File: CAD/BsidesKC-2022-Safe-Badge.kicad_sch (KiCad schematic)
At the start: 48 parts, among them J1 JTAG, J2 Conn_01x02_Female, J3 Conn_01x02_Female, J4 USB_B_Mini, J5 Conn_01x02_Female, SW1 SW_SPDT, SW2 SW_SPST, SW3 RotaryEncoder_Switch, U1 LTC4054, U2 ESP32-S2-WROVER, U3 CH330N, U4 TLV1117-33, X1 Badgelife_sao_connector_v169b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

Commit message: fixing footprint and fill
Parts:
- removed D21, D22: LED, BadgePiratesCommon:LED_Osram_Lx_P47F_D2mm_ReverseMount_Proper_Mask Only, symbol Device:LED
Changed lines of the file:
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@@
     (comment 3 "USB to Serial Connector")
-  )
-  (junction (at 55.88 158.75) (diameter 0) (color 0 0 0 0)
-  )
-  (junction (at 54.61 198.12) (diameter 0) (color 0 0 0 0)
   )
   (junction (at 36.83 198.12) (diameter 0) (color 0 0 0 0)
@@
     (stroke (width 0) (type default) (color 0 0 0 0))
   )
-  (wire (pts (xy 54.61 198.12) (xy 72.39 198.12))
-    (stroke (width 0) (type default) (color 0 0 0 0))
-  )
   (wire (pts (xy 25.4 96.52) (xy 44.45 96.52))
     (stroke (width 0) (type default) (color 0 0 0 0))
@@
     (stroke (width 0) (type default) (color 0 0 0 0))
   )
-  (wire (pts (xy 72.39 198.12) (xy 72.39 189.23))
-    (stroke (width 0) (type default) (color 0 0 0 0))
-  )
   (wire (pts (xy -30.48 173.99) (xy -12.7 173.99))
     (stroke (width 0) (type default) (color 0 0 0 0))
@@
     (stroke (width 0) (type default) (color 0 0 0 0))
   )
-  (wire (pts (xy 73.66 158.75) (xy 73.66 149.86))
-    (stroke (width 0) (type default) (color 0 0 0 0))
-  )
   (wire (pts (xy 72.39 179.07) (xy 72.39 170.18))
     (stroke (width 0) (type default) (color 0 0 0 0))
@@
   )
   (wire (pts (xy -48.26 173.99) (xy -38.1 173.99))
-    (stroke (width 0) (type default) (color 0 0 0 0))
-  )
-  (wire (pts (xy 55.88 158.75) (xy 73.66 158.75))
     (stroke (width 0) (type default) (color 0 0 0 0))
   )
@@
     )
   )
-  (global_label "IO13" (shape input) (at 81.28 149.86 0) (fields_autoplaced)
-    (effects (font (size 1.27 1.27)) (justify left))
-    (property "Intersheet References" "${INTERSHEET_REFS}" (id 0) (at 0 0 0)
-      (effects (font (size 1.27 1.27)) hide)
-    )
-  )
   (global_label "Boot" (shape input) (at 85.09 33.02 180) (fields_autoplaced)
     (effects (font (size 1.27 1.27)) (justify right))
@@
     (property "Intersheet References" "${INTERSHEET_REFS}" (id 0) (at 0 0 0)
       (effects (font (size 1.27 1.27)) hide)
-    )
-  )
-  (global_label "IO38" (shape input) (at 80.01 189.23 0) (fields_autoplaced)
-    (effects (font (size 1.27 1.27)) (justify left))
-    (property "Intersheet References" "${INTERSHEET_REFS}" (id 0) (at 86.6885 189.1506 0)
-      (effects (font (size 1.27 1.27)) (justify left) hide)
     )
   )
@@
     (pin "2")
   )
-  (symbol (lib_id "Device:LED") (at 77.47 149.86 0) (unit 1)
-    (in_bom yes) (on_board yes)
-    (property "Reference" "D22" (id 0) (at 77.2922 144.3482 0))
-    (property "Value" "LED" (id 1) (at 77.2922 146.6596 0))
-    (property "Footprint" "BadgePiratesCommon:LED_Osram_Lx_P47F_D2mm_ReverseMount_Proper_Mask Only" (id 2) (at 77.47 149.86 0)
-      (effects (font (size 1.27 1.27)) hide)
-    )
-    (property "Datasheet" "~" (id 3) (at 77.47 149.86 0)
-      (effects (font (size 1.27 1.27)) hide)
-    )
-    (pin "1")
-    (pin "2")
-  )
   (symbol (lib_id "power:GND") (at 152.4 101.6 0) (unit 1)
     (in_bom yes) (on_board yes)
@@
     (pin "2")
   )
-  (symbol (lib_id "Device:LED") (at 76.2 189.23 0) (unit 1)
-    (in_bom yes) (on_board yes)
-    (property "Reference" "D21" (id 0) (at 76.0222 183.7182 0))
-    (property "Value" "LED" (id 1) (at 76.0222 186.0296 0))
-    (property "Footprint" "BadgePiratesCommon:LED_Osram_Lx_P47F_D2mm_ReverseMount_Proper_Mask Only" (id 2) (at 76.2 189.23 0)
-      (effects (font (size 1.27 1.27)) hide)
-    )
-    (property "Datasheet" "~" (id 3) (at 76.2 189.23 0)
-      (effects (font (size 1.27 1.27)) hide)
-    )
-    (pin "1")
-    (pin "2")
-  )
   (symbol (lib_id "BadgePirates:Badgelife_sao_connector_v169bis") (at 217.17 139.7 0) (unit 1)
     (in_bom yes) (on_board yes) (fields_autoplaced)
@@
       (reference "D20") (unit 1) (value "LED") (footprint "BadgePiratesCommon:LED_Osram_Lx_P47F_D2mm_ReverseMount_Proper_Mask Only")
     )
-    (path "/9071e38a-572a-4eb6-923e-9269f884d02e"
-      (reference "D21") (unit 1) (value "LED") (footprint "BadgePiratesCommon:LED_Osram_Lx_P47F_D2mm_ReverseMount_Proper_Mask Only")
-    )
-    (path "/00000000-0000-0000-0000-0000614a349d"
-      (reference "D22") (unit 1) (value "LED") (footprint "BadgePiratesCommon:LED_Osram_Lx_P47F_D2mm_ReverseMount_Proper_Mask Only")
-    )
     (path "/00000000-0000-0000-0000-0000614dfd7a"

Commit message: adding silk layer
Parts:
- U2: value ESP32-S2-WROVER -> ESP32-S2-WROOM
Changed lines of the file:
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@@
     (in_bom yes) (on_board yes)
     (property "Reference" "U2" (id 0) (at 161.29 41.91 0))
-    (property "Value" "ESP32-S2-WROVER" (id 1) (at 162.56 44.45 0))
+    (property "Value" "ESP32-S2-WROOM" (id 1) (at 162.56 44.45 0))
     (property "Footprint" "BadgePiratesCommon:ESP32-S2-WROVER" (id 2) (at 171.45 102.87 0)
       (effects (font (size 1.27 1.27)) hide)
@@
     )
     (path "/00000000-0000-0000-0000-0000614897e3"
-      (reference "U2") (unit 1) (value "ESP32-S2-WROVER") (footprint "BadgePiratesCommon:ESP32-S2-WROVER")
+      (reference "U2") (unit 1) (value "ESP32-S2-WROOM") (footprint "BadgePiratesCommon:ESP32-S2-WROVER")
     )
     (path "/00000000-0000-0000-0000-0000615912ef"

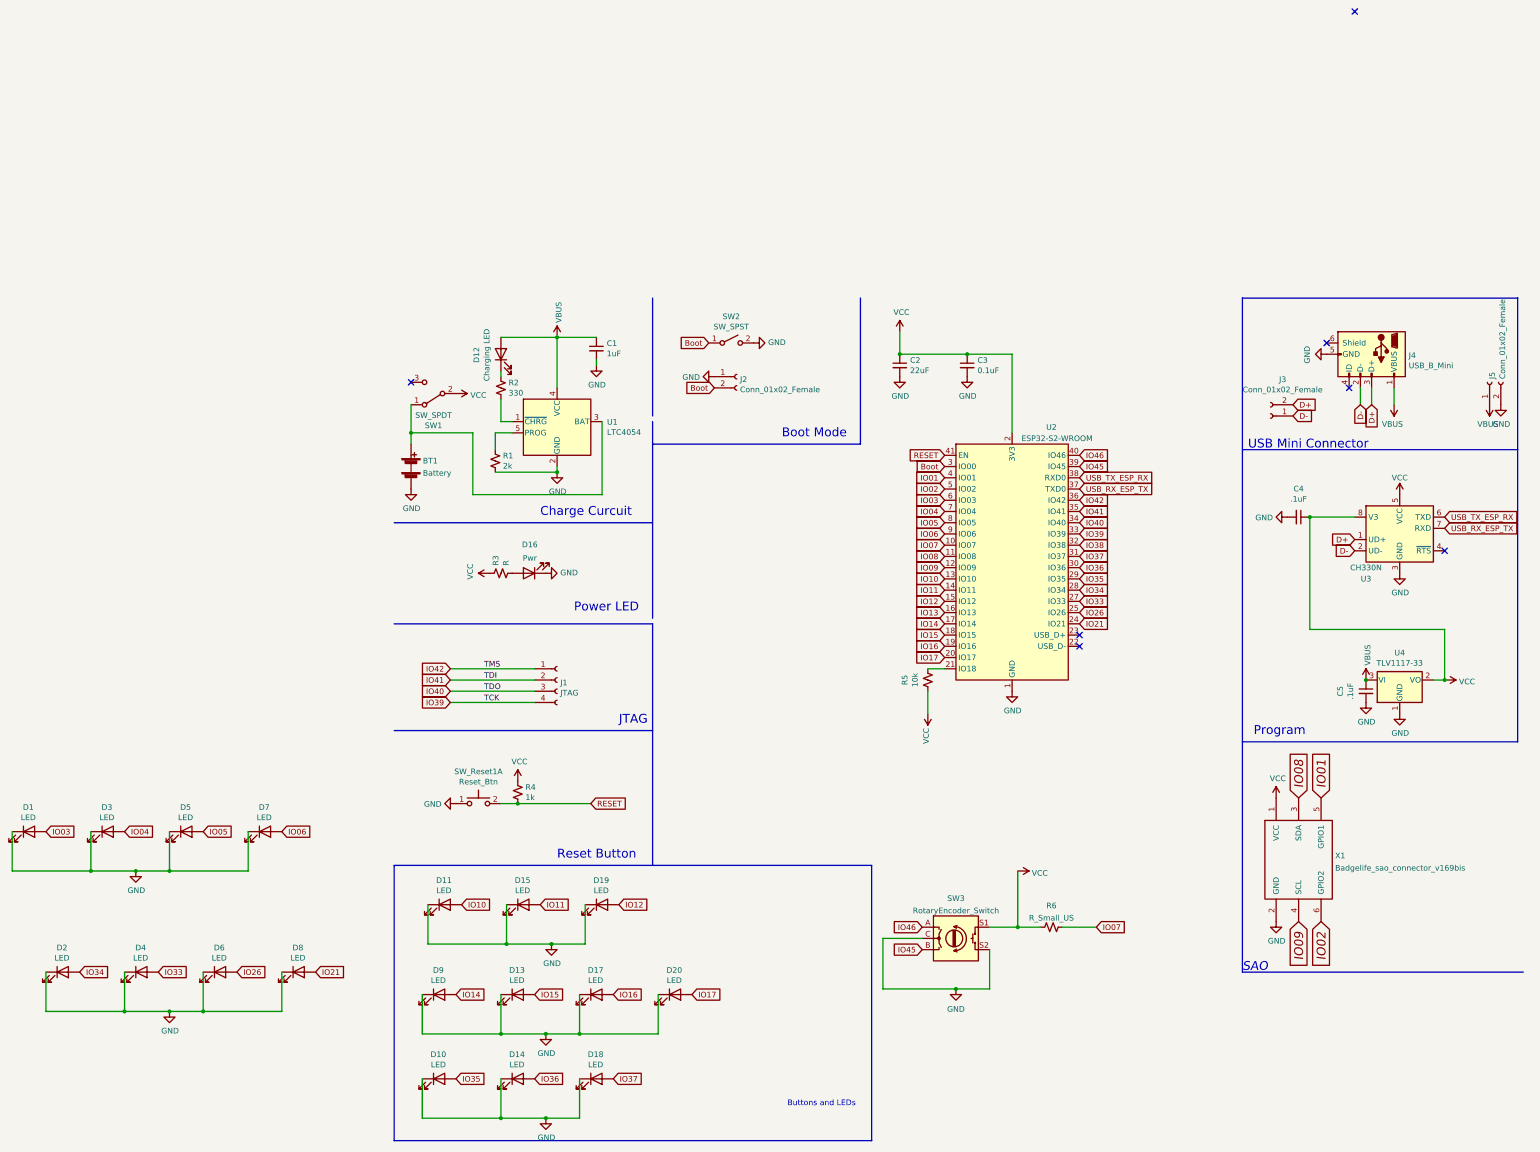
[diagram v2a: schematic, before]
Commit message: fixes
Fixing silk, and adding headers
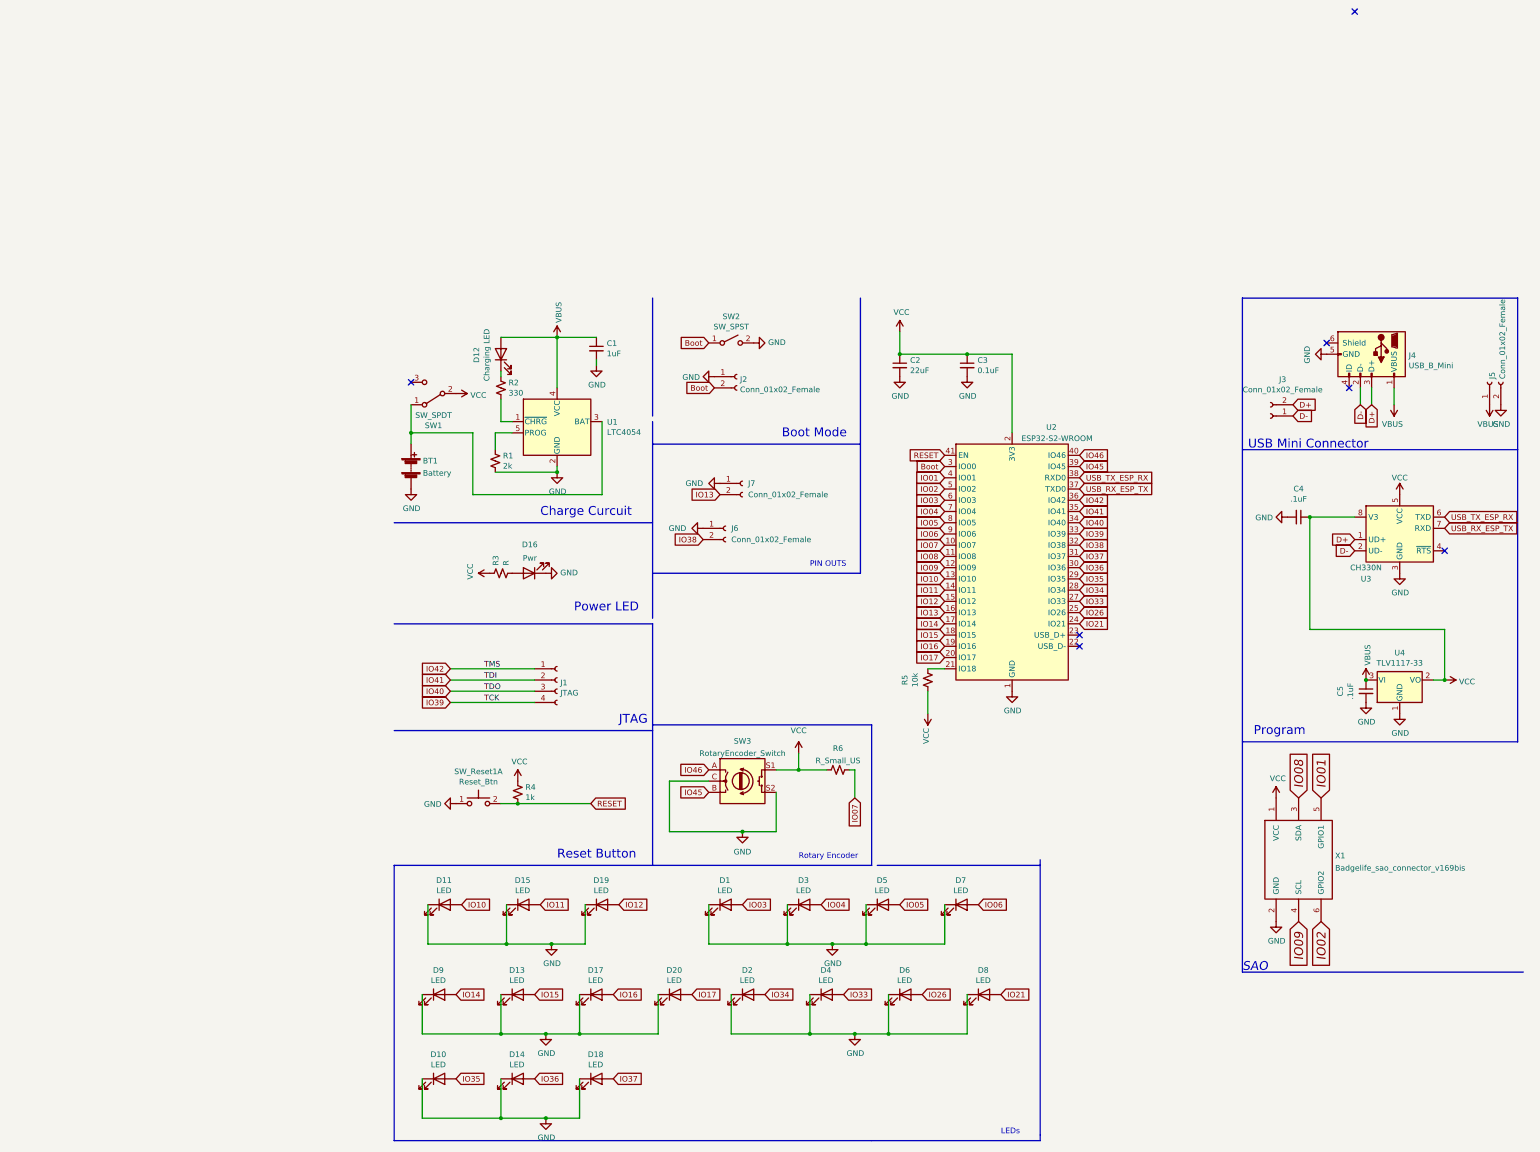
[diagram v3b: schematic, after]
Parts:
- added J6, J7: Conn_01x02_Female, Connector_PinHeader_2.54mm:PinHeader_1x02_P2.54mm_Vertical, symbol Connector:Conn_01x02_Female
- J1: footprint TestPoint:TestPoint_Pad_3.0x3.0mm -> Connector_PinHeader_2.54mm:PinHeader_1x04_P2.54mm_Vertical
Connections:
- net GND: now also J6.1 (Pin_1), J7.1 (Pin_1)
- net IO13: now also J7.2 (Pin_2)
- net IO38: now also J6.2 (Pin_2)
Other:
- note added: "LEDs"
- note added: "PIN OUTS"
- note added: "Rotary Encoder"
- note removed: "Buttons and LEDs"
- title: Prospect Boards -> BSides KC 2022 Safe
- moved on the sheet: D1, D2, D3, D4, D5, D6, D7, D8, R6, SW3

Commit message: adding R
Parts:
- added R10, R11, R12, R13, R14, R15, R16, R17, R18, R19, R20, R21, R22, R23, R24, R7, R8, R9: 1k, BadgePirates:R_1206_3216Metric, symbol Device:R_US
- C4, C5: value .1uF -> 0.1uF
- D12: value Charging LED -> Charging
- J2: value Conn_01x02_Female -> Boot Jumper
- J3: value Conn_01x02_Female -> D+ D-
- J5: value Conn_01x02_Female -> 5v GND
- J6: value Conn_01x02_Female -> IO38
- J7: value Conn_01x02_Female -> IO13
- R3: value R -> 1k
- R6: value R_Small_US -> 1k
- SW2: value SW_SPST -> Boot
- SW_Reset1: value Reset_Btn -> Reset
- X1: value Badgelife_sao_connector_v169bis -> sao_v169bis
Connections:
- net IO03: now also R7.1; no longer D1.2 (A)
- net IO04: now also R8.1; no longer D3.2 (A)
- net IO05: now also R9.1; no longer D5.2 (A)
- net IO06: now also R10.1; no longer D7.2 (A)
- net IO10: now also R11.1; no longer D11.2 (A)
- net IO11: now also R12.1; no longer D15.2 (A)
- net IO12: now also R13.1; no longer D19.2 (A)
- net IO14: now also R14.1; no longer D9.2 (A)
- net IO15: now also R15.1; no longer D13.2 (A)
- net IO16: now also R16.1; no longer D17.2 (A)
- net IO17: now also R17.1; no longer D20.2 (A)
- net IO21: now also R21.1; no longer D8.2 (A)
- net IO26: now also R20.1; no longer D6.2 (A)
- net IO33: now also R19.1; no longer D4.2 (A)
- net IO34: now also R18.1; no longer D2.2 (A)
- net IO35: now also R22.1; no longer D10.2 (A)
- net IO36: now also R23.1; no longer D14.2 (A)
- net IO37: now also R24.1; no longer D18.2 (A)
- new net: D11.2 (A), R11.2
- new net: D15.2 (A), R12.2
- new net: D19.2 (A), R13.2
- new net: D17.2 (A), R16.2
- new net: D3.2 (A), R8.2
- new net: D20.2 (A), R17.2
- new net: D13.2 (A), R15.2
- new net: D5.2 (A), R9.2
- new net: D10.2 (A), R22.2
- new net: D6.2 (A), R20.2
- new net: D9.2 (A), R14.2
- new net: D1.2 (A), R7.2
- new net: D8.2 (A), R21.2
- new net: D7.2 (A), R10.2
- new net: D4.2 (A), R19.2
- new net: D18.2 (A), R24.2
- new net: D14.2 (A), R23.2
- new net: D2.2 (A), R18.2
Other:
- moved on the sheet: C2, C3, D1, D10, D11, D13, D14, D15, D17, D18, D19, D2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

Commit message: fixing rotatry messup
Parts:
- removed J6: IO38, Connector_PinHeader_2.54mm:PinHeader_1x02_P2.54mm_Vertical, symbol Connector:Conn_01x02_Female
- removed J7: IO13, Connector_PinHeader_2.54mm:PinHeader_1x02_P2.54mm_Vertical, symbol Connector:Conn_01x02_Female
- added R16, R17: 10k, BadgePirates:R_1206_3216Metric, symbol Device:R_Small_US
- BT1: footprint BadgePiratesCommon:AA -> BadgePirates:AA
- C1, C2, C3, C4, C5: footprint BadgePiratesCommon:C_0805_2012Metric -> BadgePirates:C_0805_2012Metric
- D1: renamed from D2; footprint BadgePiratesCommon:LED_Osram_Lx_P47F_D2mm_ReverseMount_Proper_Mask Only -> BadgePirates:LED_Osram_Lx_P47F_D2mm_ReverseMount_Proper_Mask Only
- D10: renamed from D7; footprint BadgePiratesCommon:LED_Osram_Lx_P47F_D2mm_ReverseMount_Proper_Mask Only -> BadgePirates:LED_Osram_Lx_P47F_D2mm_ReverseMount_Proper_Mask Only
- D11: renamed from D10; footprint BadgePiratesCommon:LED_Osram_Lx_P47F_D2mm_ReverseMount_Proper_Mask Only -> BadgePirates:LED_Osram_Lx_P47F_D2mm_ReverseMount_Proper_Mask Only
- D12: renamed from D11; footprint BadgePiratesCommon:LED_Osram_Lx_P47F_D2mm_ReverseMount_Proper_Mask Only -> BadgePirates:LED_Osram_Lx_P47F_D2mm_ReverseMount_Proper_Mask Only
- D13: renamed from D15; footprint BadgePiratesCommon:LED_Osram_Lx_P47F_D2mm_ReverseMount_Proper_Mask Only -> BadgePirates:LED_Osram_Lx_P47F_D2mm_ReverseMount_Proper_Mask Only
- D14, D20: footprint BadgePiratesCommon:LED_Osram_Lx_P47F_D2mm_ReverseMount_Proper_Mask Only -> BadgePirates:LED_Osram_Lx_P47F_D2mm_ReverseMount_Proper_Mask Only
- D15: renamed from D19; footprint BadgePiratesCommon:LED_Osram_Lx_P47F_D2mm_ReverseMount_Proper_Mask Only -> BadgePirates:LED_Osram_Lx_P47F_D2mm_ReverseMount_Proper_Mask Only
- D16: renamed from D18; footprint BadgePiratesCommon:LED_Osram_Lx_P47F_D2mm_ReverseMount_Proper_Mask Only -> BadgePirates:LED_Osram_Lx_P47F_D2mm_ReverseMount_Proper_Mask Only
- D17: renamed from D9; footprint BadgePiratesCommon:LED_Osram_Lx_P47F_D2mm_ReverseMount_Proper_Mask Only -> BadgePirates:LED_Osram_Lx_P47F_D2mm_ReverseMount_Proper_Mask Only
- D18: renamed from D13; footprint BadgePiratesCommon:LED_Osram_Lx_P47F_D2mm_ReverseMount_Proper_Mask Only -> BadgePirates:LED_Osram_Lx_P47F_D2mm_ReverseMount_Proper_Mask Only
- D19: renamed from D17; footprint BadgePiratesCommon:LED_Osram_Lx_P47F_D2mm_ReverseMount_Proper_Mask Only -> BadgePirates:LED_Osram_Lx_P47F_D2mm_ReverseMount_Proper_Mask Only
- D2: renamed from D1; footprint BadgePiratesCommon:LED_Osram_Lx_P47F_D2mm_ReverseMount_Proper_Mask Only -> BadgePirates:LED_Osram_Lx_P47F_D2mm_ReverseMount_Proper_Mask Only
- D3: renamed from D4; footprint BadgePiratesCommon:LED_Osram_Lx_P47F_D2mm_ReverseMount_Proper_Mask Only -> BadgePirates:LED_Osram_Lx_P47F_D2mm_ReverseMount_Proper_Mask Only
- D5: renamed from D3; footprint BadgePiratesCommon:LED_Osram_Lx_P47F_D2mm_ReverseMount_Proper_Mask Only -> BadgePirates:LED_Osram_Lx_P47F_D2mm_ReverseMount_Proper_Mask Only
- D7: renamed from D6; footprint BadgePiratesCommon:LED_Osram_Lx_P47F_D2mm_ReverseMount_Proper_Mask Only -> BadgePirates:LED_Osram_Lx_P47F_D2mm_ReverseMount_Proper_Mask Only
- D8: renamed from D5; footprint BadgePiratesCommon:LED_Osram_Lx_P47F_D2mm_ReverseMount_Proper_Mask Only -> BadgePirates:LED_Osram_Lx_P47F_D2mm_ReverseMount_Proper_Mask Only
- D9: renamed from D8; footprint BadgePiratesCommon:LED_Osram_Lx_P47F_D2mm_ReverseMount_Proper_Mask Only -> BadgePirates:LED_Osram_Lx_P47F_D2mm_ReverseMount_Proper_Mask Only
- J2, J3, J5: footprint BadgePiratesCommon:PinHeader_1x02_P2.54mm_Vertical -> BadgePirates:PinHeader_1x02_P2.54mm_Vertical
- J4: footprint BadgePiratesCommon:USB_Micro-B_Wuerth -> BadgePirates:USB_Micro-B_Wuerth
- R21: renamed from R6; value 1k -> 10k; footprint BadgePiratesCommon:R_1206_3216Metric -> BadgePirates:R_1206_3216Metric
- R25: renamed from R5; footprint BadgePiratesCommon:R_1206_3216Metric -> BadgePirates:R_1206_3216Metric
- R26: renamed from R4; footprint BadgePiratesCommon:R_1206_3216Metric -> BadgePirates:R_1206_3216Metric
- R3: renamed from R1; footprint BadgePiratesCommon:R_1206_3216Metric -> BadgePirates:R_1206_3216Metric
- R5: renamed from R2; footprint BadgePiratesCommon:R_1206_3216Metric -> BadgePirates:R_1206_3216Metric
- R6: renamed from R3; footprint BadgePiratesCommon:R_1206_3216Metric -> BadgePirates:R_1206_3216Metric
- SW1: footprint BadgePiratesCommon:SW_SPDT_PCM12 -> BadgePirates:SW_SPDT_PCM12
- SW2, SW_Reset1: footprint BadgePiratesCommon:Switch_Tactile_SMD_B3U-1000P-BPVersion -> BadgePirates:Switch_Tactile_SMD_B3U-1000P-BPVersion
- SW3: footprint Rotary_Encoder:RotaryEncoder_Alps_EC12E-Switch_Vertical_H20mm_CircularMountingHoles -> Rotary_Encoder:RotaryEncoder_Alps_EC11E_Vertical_H20mm_CircularMountingHoles
- U1: footprint BadgePiratesCommon:LTC4054 -> BadgePirates:LTC4054
- U2: footprint BadgePiratesCommon:ESP32-S2-WROVER -> BadgePirates:ESP32-S2-WROOM
- U3: footprint BadgePiratesCommon:SOIC-8-1EP_W3.9mm -> BadgePirates:SOIC-8-1EP_W3.9mm
- U4: footprint BadgePiratesCommon:SOT-223 -> BadgePirates:SOT-223
- X1: footprint BadgePiratesCommon:Badgelife-SAOv169-SAO_Side_B.SLK -> BadgePirates:Badgelife-SAOv169-SAO_Side_B.SLK
- renumbered D12 to D4, D16 to D6, R18 to R1, R21 to R10, R10 to R11, R22 to R12, R11 to R13, R12 to R14, R23 to R15, R13 to R18, R24 to R19, R7 to R2, R14 to R20, R15 to R22, R16 to R23, R17 to R24, R19 to R4, R8 to R7, R20 to R8
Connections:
- net IO07: now also R21.2, SW3.S1; no longer R21.1
- net IO13: now also SW3.B, R17.1
- net IO38: now also SW3.A, R16.1
- net VCC: now also R21.1, R16.2, R17.2; no longer R21.2, SW3.S1
- net IO45: no longer names the net of U2.39 (IO45)
- net IO45: no longer SW3.B
- net IO46: no longer names the net of U2.40 (IO46)
- net IO46: no longer SW3.A
- no-connect marks 7 -> 8
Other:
- note removed: "PIN OUTS"
- moved on the sheet: R21, SW3
